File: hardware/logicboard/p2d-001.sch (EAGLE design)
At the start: 68 parts, among them IC1 74LS06N, IC2 4066N, IC3 MAX3468CPA, J1 MKR, J10 THS, J2 GPIO, J3 Vcc, J4 RLY, J5 SPI, J6 LED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

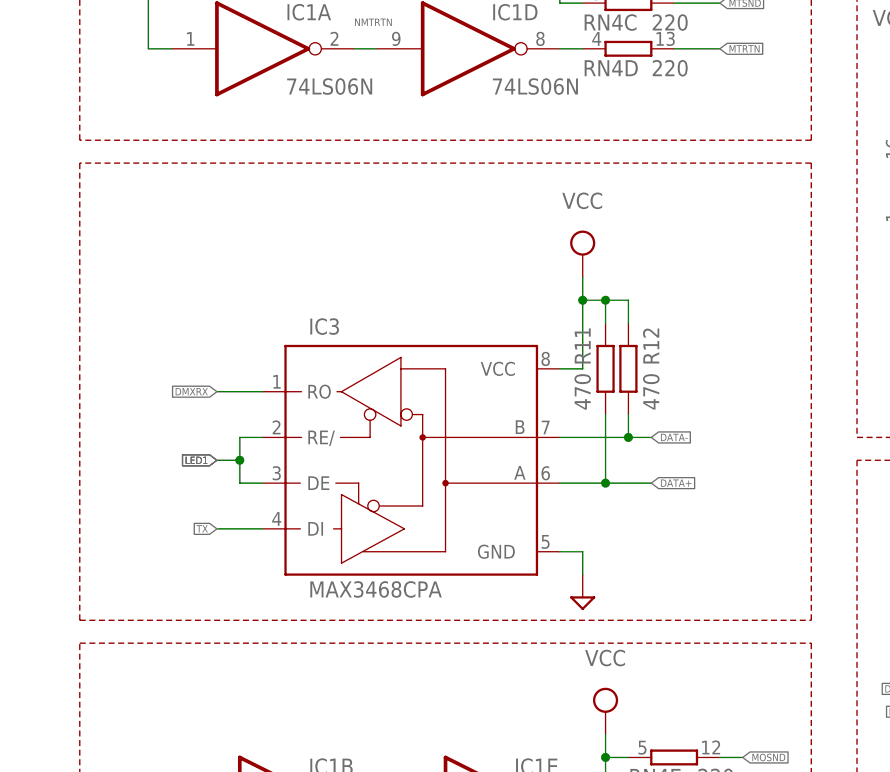
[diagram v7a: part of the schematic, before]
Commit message: Now DMX's Data- has pull-down R., not pull-up.
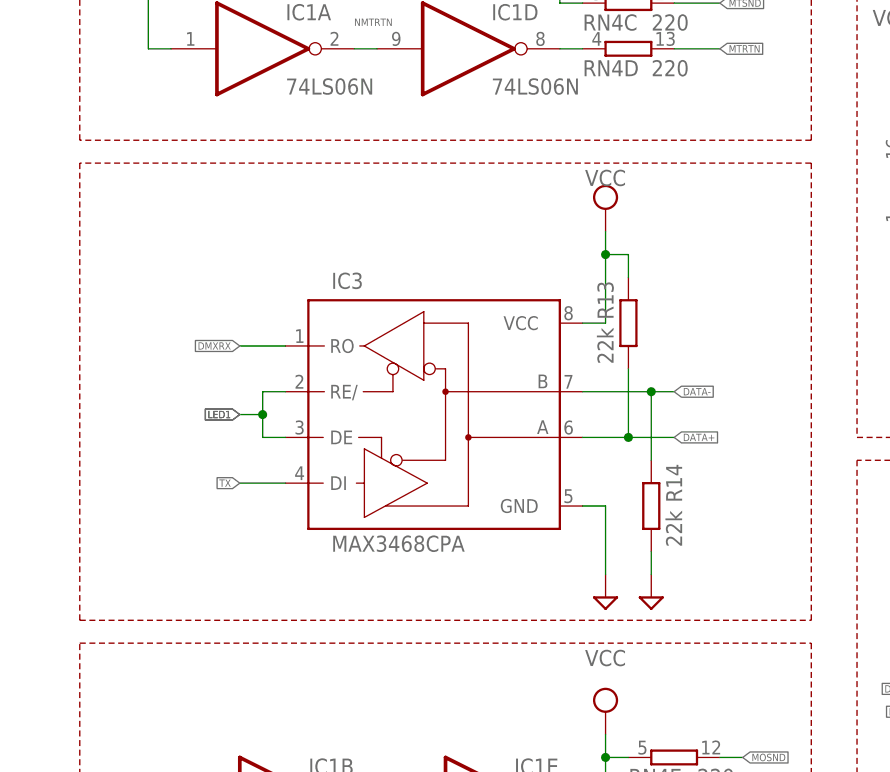
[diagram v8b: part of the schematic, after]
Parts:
- removed R11, R12: 470, resistor:R-EU_0204/5
- added R13, R14: 22k, resistor:R-EU_0204/5
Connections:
- net DATA+: now also R13.1; no longer R11.1
- net DATA-: now also R14.2; no longer R12.1
- net GND: now also R14.1
- net VCC: now also R13.2; no longer R11.2, R12.2
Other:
- moved on the sheet: IC3
